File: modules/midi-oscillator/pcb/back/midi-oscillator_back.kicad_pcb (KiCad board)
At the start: 2 copper layers, 38.2 x 110.2 mm, 18 parts, among them J1 DEBUG, J2 Conn_02x08_Odd_Even, J3 Conn_01x14, U1 Pico, U2 MCP4822, U3 MCP4822, U4 24LC512

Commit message: modules: midi-oscillator: schematic improvements, added pdf
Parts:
- J1: value DEBUG -> JST XH 1x5
- J2: value Conn_02x08_Odd_Even -> IDC Header 2x8
- J3: value Conn_01x14 -> Pin Socket 1x14
- U1: value Pico -> Raspberry Pi Pico
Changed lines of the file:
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@@
   (page A4)
   (title_block
-    (title "midi-controller back board")
+    (title "midi-controller back")
     (date 2021-12-15)
     (rev 1.0)
@@
       (effects (font (size 1 1) (thickness 0.15)) (justify mirror))
     )
-    (fp_text value Pico (at 0 -2.159) (layer B.Fab)
+    (fp_text value "Raspberry Pi Pico" (at 0 -2.159) (layer B.Fab)
       (effects (font (size 1 1) (thickness 0.15)) (justify mirror))
     )
@@
       (effects (font (size 1 1) (thickness 0.15)))
     )
-    (fp_text value Conn_01x14 (at 0 35.79) (layer F.Fab)
+    (fp_text value "Pin Socket 1x14" (at 0 35.79) (layer F.Fab)
       (effects (font (size 1 1) (thickness 0.15)))
     )
@@
       (effects (font (size 1 1) (thickness 0.15)) (justify mirror))
     )
-    (fp_text value Conn_02x08_Odd_Even (at 1.27 -23.88 270) (layer B.Fab)
+    (fp_text value "IDC Header 2x8" (at 1.27 -23.88 270) (layer B.Fab)
       (effects (font (size 1 1) (thickness 0.15)) (justify mirror))
     )
@@
       (effects (font (size 1 1) (thickness 0.15)) (justify mirror))
     )
-    (fp_text value DEBUG (at 5 -4.6 270) (layer B.Fab)
-      (effects (font (size 1 1) (thickness 0.15)) (justify mirror))
-    )
+    (fp_text value "JST XH 1x5" (at 5 -4.6 270) (layer B.Fab)
+      (effects (font (size 1 1) (thickness 0.15)) (justify mirror))
+    )

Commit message: modules: midi-oscillator: back: upgrade to kicad 6
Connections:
- J2 pad 13: (no net) -> unconnected-(J2-Pad13)
- J2 pad 14: (no net) -> unconnected-(J2-Pad14)
- J2 pad 15: (no net) -> unconnected-(J2-Pad15)
- J2 pad 16: (no net) -> unconnected-(J2-Pad16)
- U1 pad 1: Net-(U1-Pad1) -> unconnected-(U1-Pad1)
- U1 pad 10: Net-(U1-Pad10) -> unconnected-(U1-Pad10)
- U1 pad 2: Net-(U1-Pad2) -> unconnected-(U1-Pad2)
- U1 pad 27: Net-(U1-Pad27) -> unconnected-(U1-Pad27)
- U1 pad 29: Net-(U1-Pad29) -> unconnected-(U1-Pad29)
- U1 pad 30: Net-(U1-Pad30) -> unconnected-(U1-Pad30)
- U1 pad 31: Net-(U1-Pad31) -> unconnected-(U1-Pad31)
- U1 pad 32: Net-(U1-Pad32) -> unconnected-(U1-Pad32)
- U1 pad 34: Net-(U1-Pad34) -> unconnected-(U1-Pad34)
- U1 pad 35: Net-(U1-Pad35) -> unconnected-(U1-Pad35)
- U1 pad 37: Net-(U1-Pad37) -> unconnected-(U1-Pad37)
- U1 pad 4: Net-(U1-Pad4) -> unconnected-(U1-Pad4)
- U1 pad 40: Net-(U1-Pad40) -> unconnected-(U1-Pad40)
- U1 pad 5: Net-(U1-Pad5) -> unconnected-(U1-Pad5)
- U1 pad 6: Net-(U1-Pad6) -> unconnected-(U1-Pad6)
- U1 pad 9: Net-(U1-Pad9) -> unconnected-(U1-Pad9)
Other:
- net class Default removed

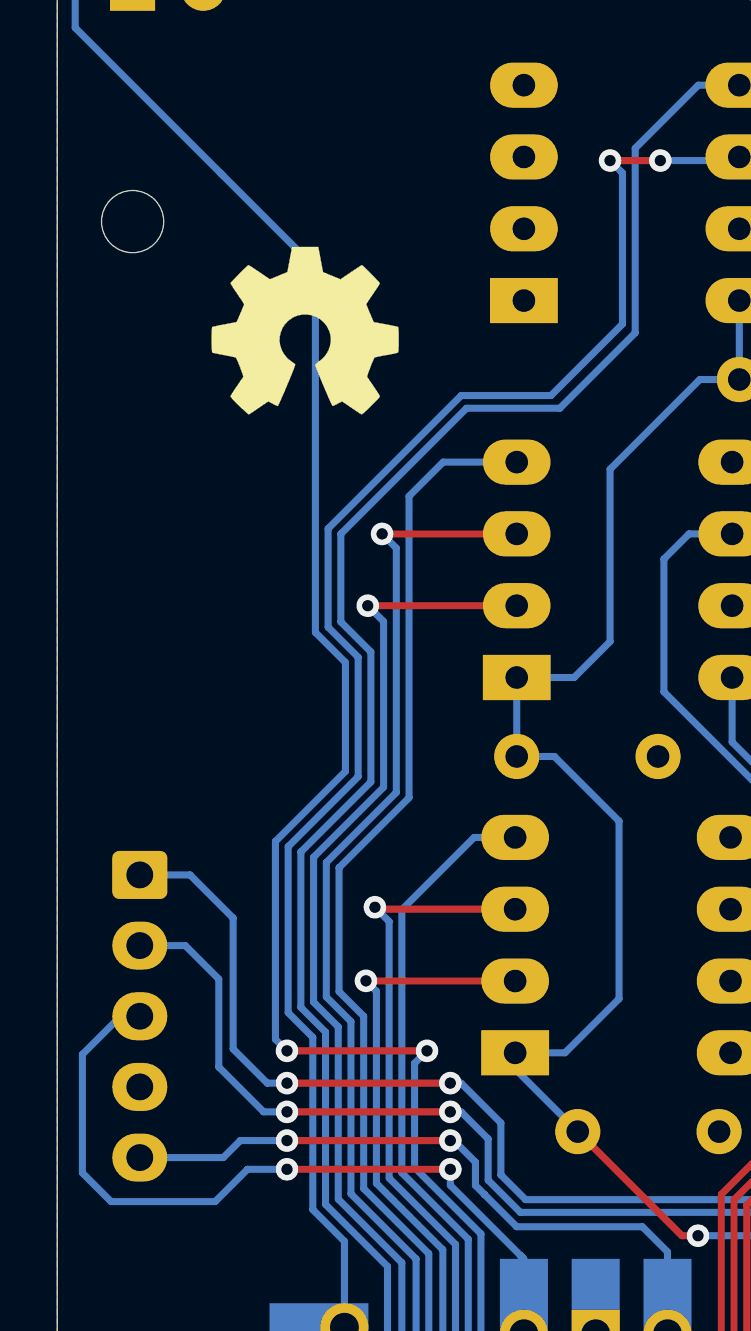
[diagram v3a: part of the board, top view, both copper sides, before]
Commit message: modules: midi-oscillator: back: remove unconnected nets
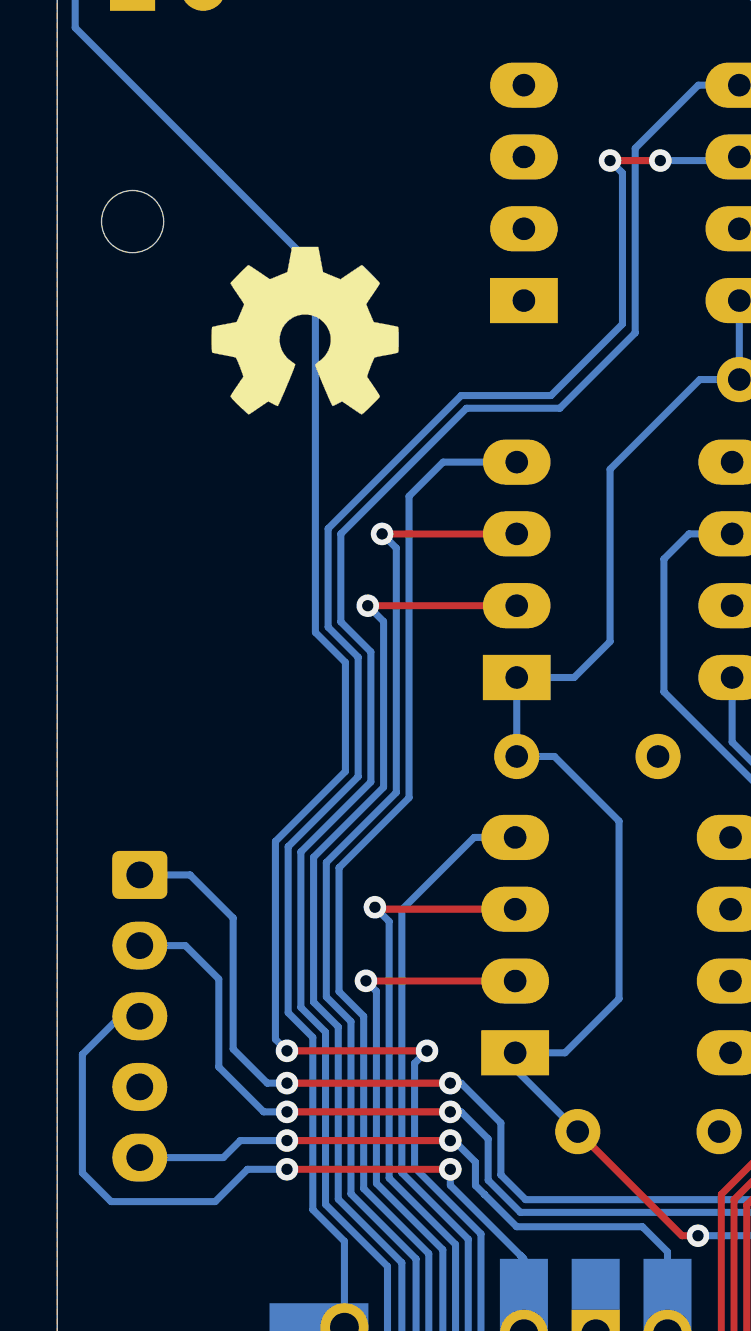
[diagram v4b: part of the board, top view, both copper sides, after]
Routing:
- net DBG_SWDIO: track 24.7 -> 23.9 mm
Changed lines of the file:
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@@
   (segment (start 139.827 136.144) (end 139.827 101.22041) (width 0.25) (layer "B.Cu") (net 1))
   (segment (start 139.827 101.22041) (end 139.82149 101.2149) (width 0.25) (layer "B.Cu") (net 1))
-  (segment (start 130.302 89.676225) (end 130.373225 89.605) (width 0.25) (layer "B.Cu") (net 1))
   (segment (start 131.7625 79.121) (end 130.429 79.121) (width 0.25) (layer "B.Cu") (net 1))
   (segment (start 130.373225 90.177725) (end 132.588 92.3925) (width 0.25) (layer "B.Cu") (net 1))
@@
   (segment (start 145.288 70.358) (end 148.717 70.358) (width 0.25) (layer "F.Cu") (net 7))
   (segment (start 141.224 74.422) (end 145.288 70.358) (width 0.25) (layer "F.Cu") (net 7))
-  (segment (start 128.651 132.334) (end 128.651 132.334) (width 0.25) (layer "F.Cu") (net 7))
   (segment (start 137.668 123.317) (end 137.668 94.615) (width 0.25) (layer "F.Cu") (net 7))
   (segment (start 137.668 94.615) (end 141.224 91.059) (width 0.25) (layer "F.Cu") (net 7))
@@
   (segment (start 137.287 45.466) (end 137.287 46.5455) (width 0.25) (layer "B.Cu") (net 12))
   (segment (start 137.287 46.5455) (end 139.7635 49.022) (width 0.25) (layer "B.Cu") (net 12))
-  (segment (start 119.9515 58.4835) (end 120.015 58.547) (width 0.25) (layer "B.Cu") (net 12))
   (segment (start 123.305981 61.837981) (end 119.9515 58.4835) (width 0.25) (layer "B.Cu") (net 12))
   (segment (start 126.5555 124.0155) (end 126.5555 121.73091) (width 0.25) (layer "B.Cu") (net 12))
@@
   (segment (start 129.286 94.61641) (end 129.286 94.615) (width 0.25) (layer "B.Cu") (net 13))
   (segment (start 120.048 93.312) (end 120.65 92.71) (width 0.25) (layer "B.Cu") (net 13))
-  (segment (start 117.889 93.312) (end 117.094 93.312) (width 0.25) (layer "B.Cu") (net 13))
   (segment (start 128.9685 93.472) (end 128.2065 92.71) (width 0.25) (layer "B.Cu") (net 13))
   (segment (start 128.0795 93.726) (end 122.301 93.726) (width 0.25) (layer "F.Cu") (net 14))

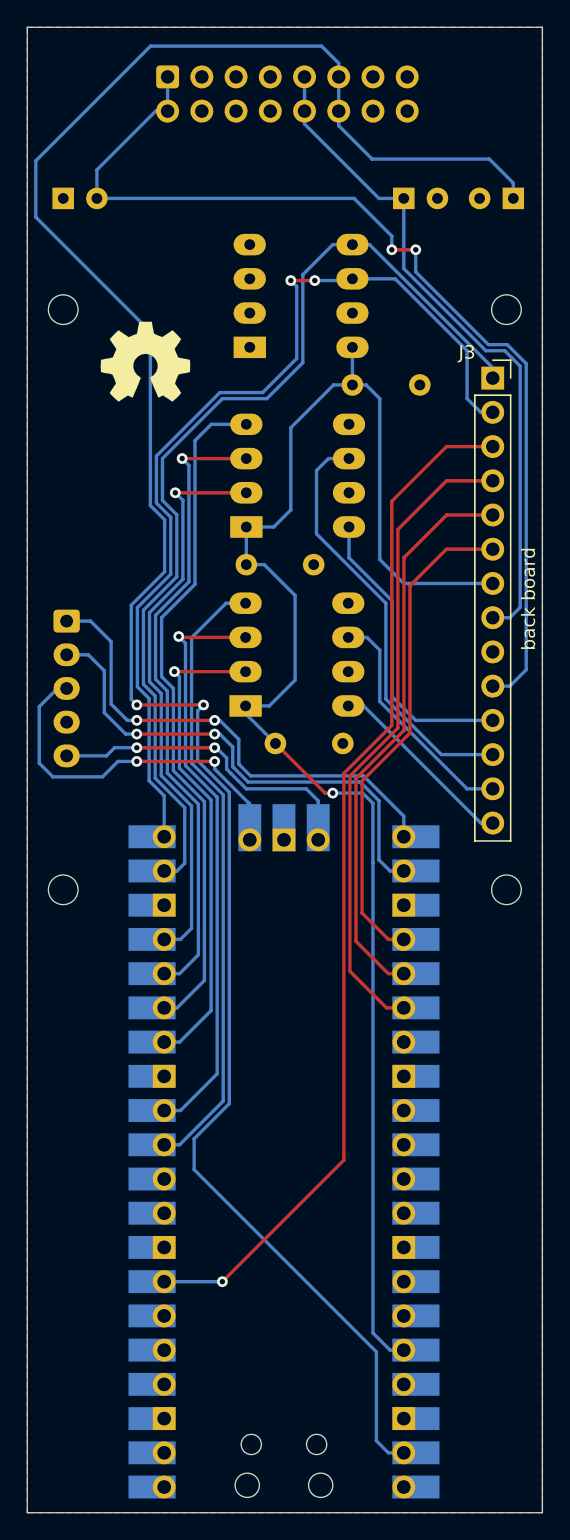
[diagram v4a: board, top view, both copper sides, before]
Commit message: modules: midi-oscillator: back: new revision 1.1
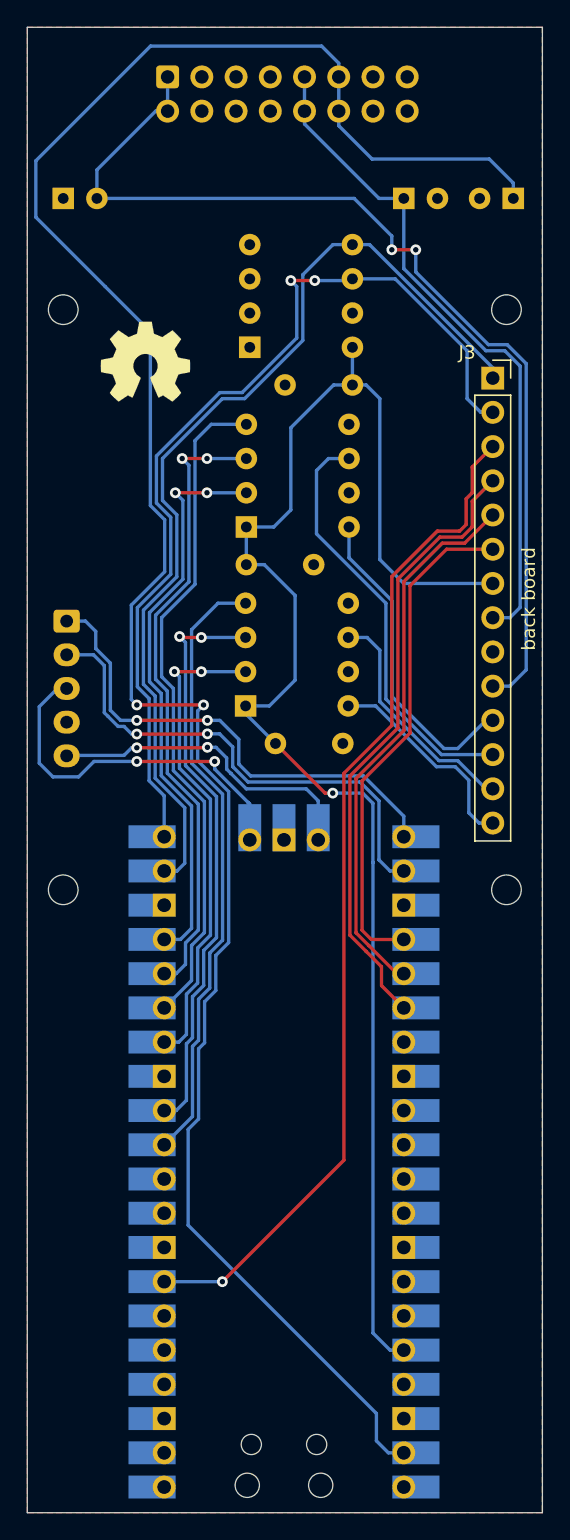
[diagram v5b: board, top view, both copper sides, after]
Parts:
- U2, U3, U4: footprint Package_DIP:DIP-8_W7.62mm_LongPads -> Package_DIP:DIP-8_W7.62mm
- turned C3 to 180 degrees
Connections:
- net +3V3 renamed +3.3V
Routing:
- net ENC_BT: track 47.9 -> 46.1 mm
- net DAC_CH1: track 22.1 -> 23.8 mm
- net ENC_B: track 42.4 -> 41.0 mm
- net DAC_CH3: track 14.3 -> 15.7 mm
- net MIDI_RX: track 76.6 -> 75.6 mm
- net I2C_SDA: track 74.0 -> 73.0 mm
- net I2C_SCL: track 71.1 -> 70.3 mm
- net ENC_A: track 36.9 -> 37.7 mm
- net DAC1_DO: track 50.5 -> 50.0 mm
- net DAC2_SCK: track 43.7 -> 43.4 mm, vias 1 -> 2
- net DAC1_SCK: track 47.3 -> 47.1 mm, vias 1 -> 2
- net DAC2_CS: track 36.0 -> 35.9 mm, vias 1 -> 2
- net DAC1_CS: vias 1 -> 2
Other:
- board text added: "midi-oscillator r1.1"
- board text removed: "midi-oscillator r1.0"
